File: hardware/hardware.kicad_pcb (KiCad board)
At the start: 2 copper layers, 160 x 160 mm, 32 parts, among them U1 MGC3130-I_MQ, U2 STM32F103C8Tx

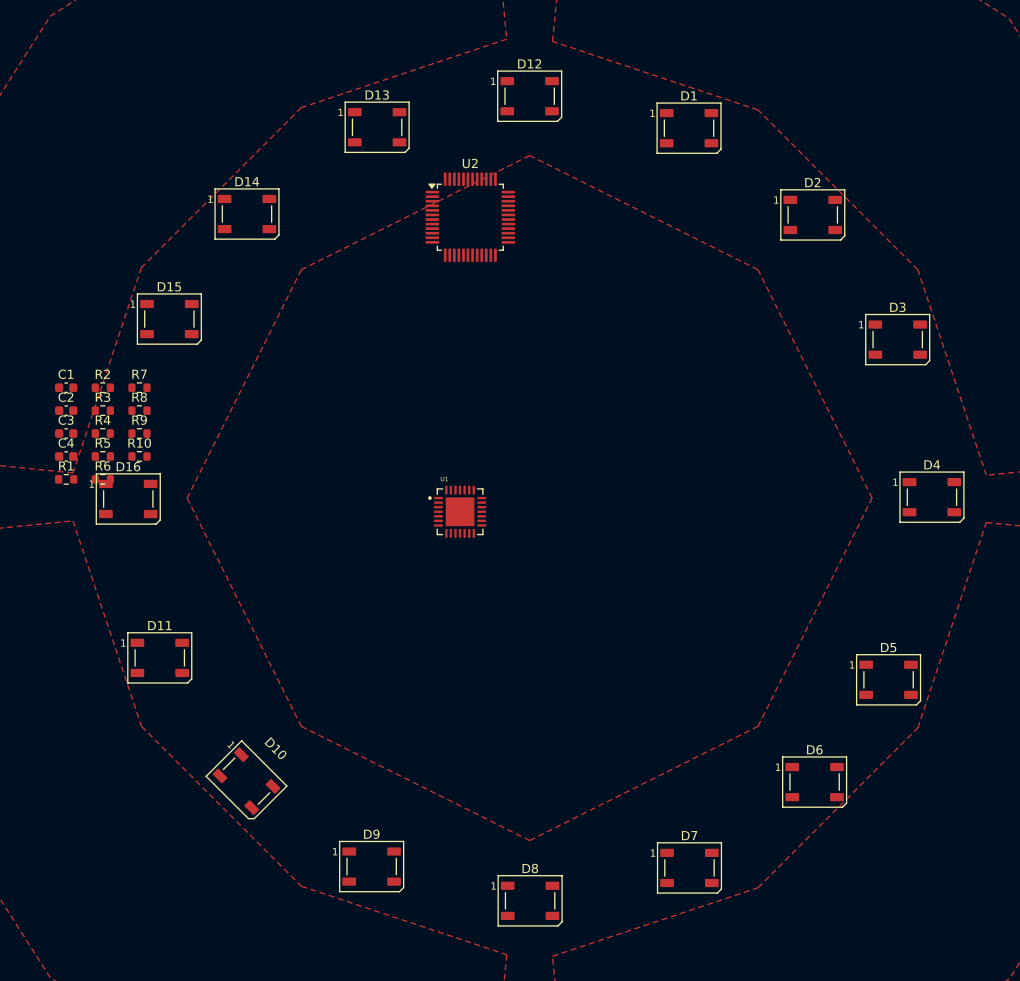
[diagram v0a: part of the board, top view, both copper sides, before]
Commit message: update sensor connections
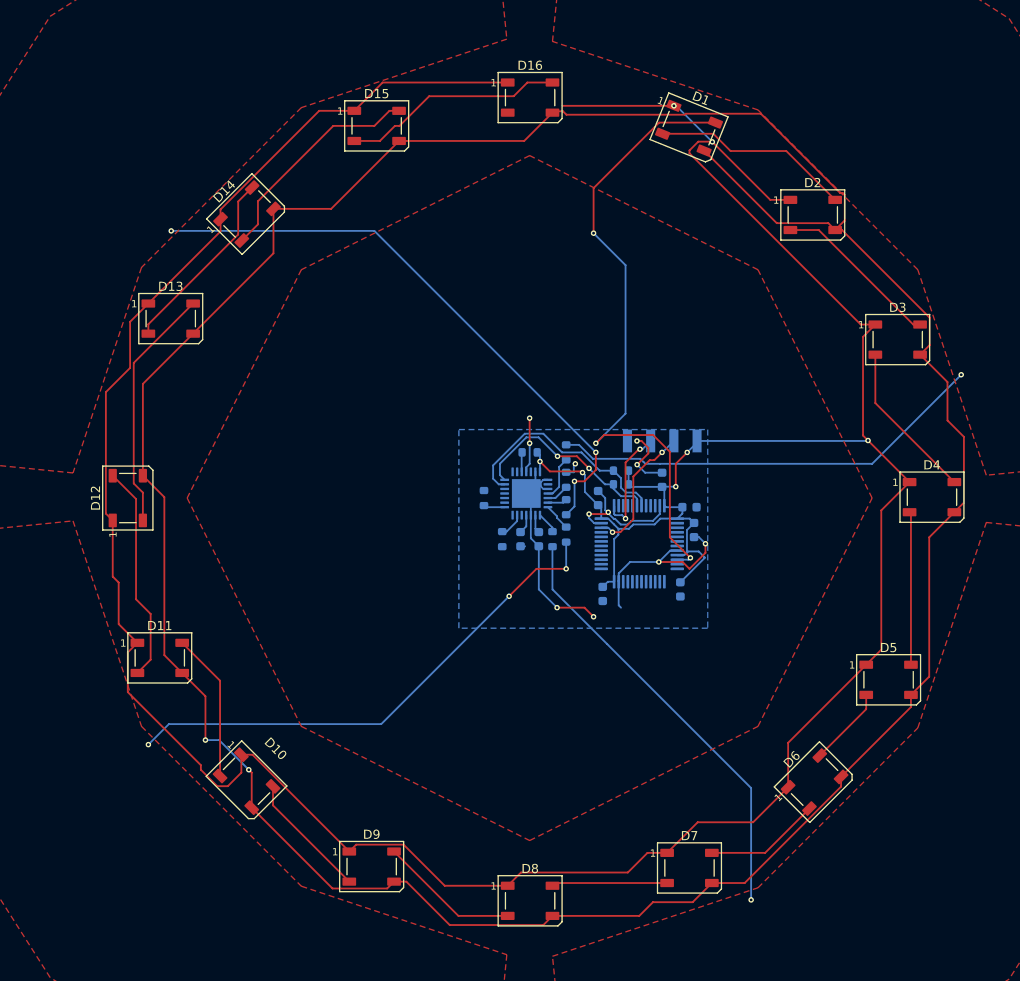
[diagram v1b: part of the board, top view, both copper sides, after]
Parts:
- added C5: 2.2uf, Capacitor_SMD:C_0603_1608Metric, B.Cu at (168.0, 103.5)
- added C6: 2.2uf, Capacitor_SMD:C_0603_1608Metric, B.Cu at (167.5, 101.0)
- added C7: 2.2uf, Capacitor_SMD:C_0603_1608Metric, B.Cu at (158.0, 110.5)
- added C8: 2.2uf, Capacitor_SMD:C_0603_1608Metric, B.Cu at (166.5, 110.0)
- added J1: Conn_01x04, Connector_Harwin:Harwin_M20-89004xx_1x04_P2.54mm_Horizontal, B.Cu at (164.5, 88.2)
- C1, C2, C3, C4, R1, R10, R2, R3, R4, R5, R6, R7, R8, R9, U1, U2: moved to B.Cu
- moved C4 65.3 mm to (164.5, 98.0), turned to -90 degrees
- moved D12 62.2 mm to (106.0, 100.0), turned to 90 degrees
- moved D16 62.2 mm to (150.1, 56.1)
- moved C3 58.7 mm to (157.5, 100.0), turned to -90 degrees
- moved C1 54.3 mm to (151.0, 104.5), turned to 90 degrees
- moved R7 53.8 mm to (160.0, 98.5), turned to 180 degrees
- moved R1 53.6 mm to (152.5, 104.5), turned to -90 degrees
- moved R10 52.7 mm to (160.0, 97.0), turned to 180 degrees
- moved C2 51.7 mm to (149.0, 104.5), turned to 90 degrees
- moved R5 51.5 mm to (154.0, 104.0), turned to -90 degrees
- moved R4 51.4 mm to (154.0, 101.0), turned to -90 degrees
- moved R3 51.3 mm to (154.0, 98.0), turned to 90 degrees
- moved R2 51.2 mm to (154.0, 95.0), turned to -90 degrees
- moved R6 46.8 mm to (150.0, 95.0), turned to 180 degrees
- moved R9 41.4 mm to (147.0, 104.5), turned to 90 degrees
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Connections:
- R1 pad 2: CENTER -> WEST
- R2 pad 1: WEST -> NORTH
- R3 pad 2: SOUTH -> CENTER
- R4 pad 2: NORTH -> EAST
- R5 pad 2: EAST -> SOUTH
- U2 pad 1: unconnected-(U2-VBAT-Pad1) -> +3V3
- U2 pad 10: unconnected-(U2-PA0-Pad10) -> WS2812
- U2 pad 23: Net-(U2-VSS-Pad23) -> GND
- U2 pad 24: unconnected-(U2-VDD-Pad24) -> +3V3
- U2 pad 34: unconnected-(U2-PA13-Pad34) -> SWDIO
- U2 pad 35: Net-(U2-VSS-Pad23) -> GND
- U2 pad 36: unconnected-(U2-VDD-Pad36) -> +3V3
- U2 pad 37: unconnected-(U2-PA14-Pad37) -> SWCLK
- U2 pad 47: Net-(U2-VSS-Pad23) -> GND
- U2 pad 48: unconnected-(U2-VDD-Pad48) -> +3V3
- U2 pad 8: unconnected-(U2-VSSA-Pad8) -> GND
- U2 pad 9: unconnected-(U2-VDDA-Pad9) -> +3V3
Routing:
- net +3V3: track 0.00 -> 387.3 mm, vias 0 -> 7
- net GND: track 0.00 -> 386.2 mm, vias 0 -> 10
- net WS2812: track 0.00 -> 70.4 mm, vias 0 -> 3
- net EAST: track 0.00 -> 65.4 mm, vias 0 -> 3
- net SOUTH: track 0.00 -> 56.6 mm, vias 0 -> 3
- net NORTH: track 0.00 -> 48.1 mm, vias 0 -> 1
- net WEST: track 0.00 -> 47.7 mm, vias 0 -> 1
- net Net-(D12-DOUT): track 0.00 -> 26.9 mm
- net SDA: track 0.00 -> 25.0 mm
- net Net-(D14-DOUT): track 0.00 -> 24.7 mm
- net Net-(D15-DOUT): track 0.00 -> 24.4 mm
- net Net-(D11-DOUT): track 0.00 -> 23.9 mm
- net SCL: track 0.00 -> 22.0 mm, vias 0 -> 2
- net Net-(D1-DOUT): track 0.00 -> 21.9 mm
- net Net-(D13-DOUT): track 0.00 -> 20.7 mm
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- added copper zone on F.Cu, net EAST
- added copper zone on B.Cu, net GND
- added copper zone on F.Cu, net SOUTH
- added copper zone on F.Cu, net WEST
